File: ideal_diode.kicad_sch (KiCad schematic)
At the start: 5 parts, among them Q1 BSC059N04LS6, U2 LM74700

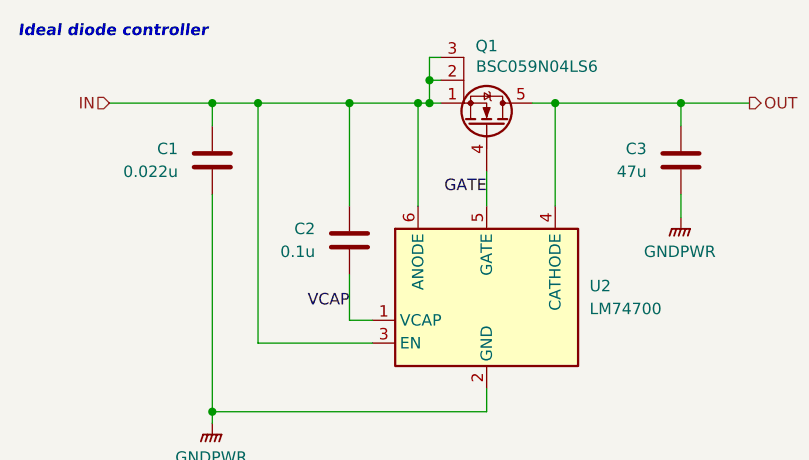
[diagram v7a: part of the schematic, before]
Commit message: Reannotate schematic
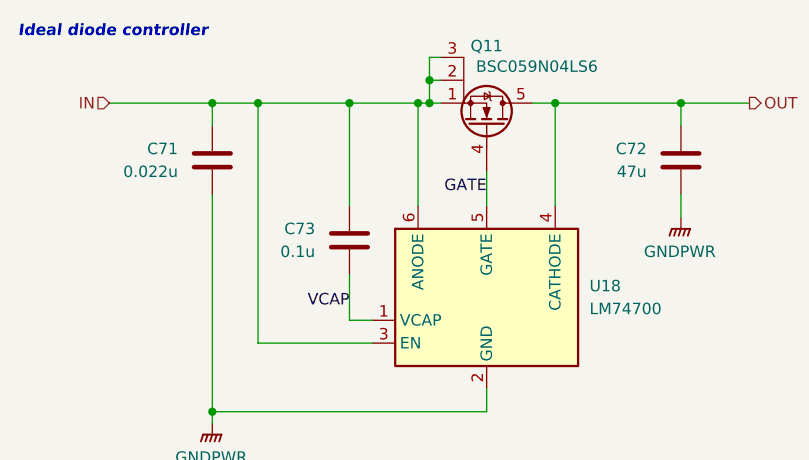
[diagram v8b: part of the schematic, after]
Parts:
- renumbered C1 to C71, C3 to C72, C2 to C73, Q1 to Q11, U2 to U18
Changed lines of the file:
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@@
 		(on_board yes)
 		(dnp no)
-		(property "Reference" "C3"
+		(property "Reference" "C72"
 			(at 121.92 36.8299 0)
 			(effects
@@
 			(project "Ideal Diode Rev1"
 				(path "/6197145b-e7d4-44cc-9d90-537b6501bf60/130ec867-c4fa-4318-bea9-b8fc517d0b0a"
-					(reference "C3")
+					(reference "C72")
 					(unit 1)
 				)
@@
 		(on_board yes)
 		(dnp no)
-		(property "Reference" "C1"
+		(property "Reference" "C71"
 			(at 69.85 36.8299 0)
 			(effects
@@
 			(project "Ideal Diode Rev1"
 				(path "/6197145b-e7d4-44cc-9d90-537b6501bf60/130ec867-c4fa-4318-bea9-b8fc517d0b0a"
-					(reference "C1")
+					(reference "C71")
 					(unit 1)
 				)
@@
 		(dnp no)
 		(fields_autoplaced yes)
-		(property "Reference" "#PWR0107"
+		(property "Reference" "#PWR0105"
 			(at 73.66 72.39 0)
 			(effects
@@
 			(project "Ideal Diode Rev1"
 				(path "/6197145b-e7d4-44cc-9d90-537b6501bf60/130ec867-c4fa-4318-bea9-b8fc517d0b0a"
-					(reference "#PWR0107")
+					(reference "#PWR0105")
 					(unit 1)
 				)
@@
 		(on_board yes)
 		(dnp no)
-		(property "Reference" "C2"
+		(property "Reference" "C73"
 			(at 85.09 45.7199 0)
 			(effects
@@
 			(project "Ideal Diode Rev1"
 				(path "/6197145b-e7d4-44cc-9d90-537b6501bf60/130ec867-c4fa-4318-bea9-b8fc517d0b0a"
-					(reference "C2")
+					(reference "C73")
 					(unit 1)
 				)
@@
 		(on_board yes)
 		(dnp no)
-		(property "Reference" "Q1"
+		(property "Reference" "Q11"
 			(at 104.14 25.4 90)
 			(effects
@@
 			(project "Ideal Diode Rev1"
 				(path "/6197145b-e7d4-44cc-9d90-537b6501bf60/130ec867-c4fa-4318-bea9-b8fc517d0b0a"
-					(reference "Q1")
+					(reference "Q11")
 					(unit 1)
 				)
@@
 		(dnp no)
 		(fields_autoplaced yes)
-		(property "Reference" "U2"
+		(property "Reference" "U18"
 			(at 115.57 52.0699 0)
 			(effects
@@
 			(project "Ideal Diode Rev1"
 				(path "/6197145b-e7d4-44cc-9d90-537b6501bf60/130ec867-c4fa-4318-bea9-b8fc517d0b0a"
-					(reference "U2")
+					(reference "U18")
 					(unit 1)
 				)
@@
 		(dnp no)
 		(fields_autoplaced yes)
-		(property "Reference" "#PWR0111"
+		(property "Reference" "#PWR0104"
 			(at 125.73 49.53 0)
 			(effects
@@
 			(project "Ideal Diode Rev1"
 				(path "/6197145b-e7d4-44cc-9d90-537b6501bf60/130ec867-c4fa-4318-bea9-b8fc517d0b0a"
-					(reference "#PWR0111")
-					(unit 1)
-				)
+					(reference "#PWR0104")
+					(unit 1)
+				)
